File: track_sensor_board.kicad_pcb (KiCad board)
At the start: 2 copper layers, 111.8 x 96.5 mm, 30 parts, among them J1 Barrel_Jack, J10 Screw_Terminal_01x02, J11 Screw_Terminal_01x02, J2 10-18-1032, J3 10-18-1032, J4 10-18-1032, J5 10-18-1032, J6 10-18-1032, J7 10-18-1032, J8 10-18-1032, J9 10-18-1032, SW1 SW_DIP_x04, U1 MCP23017_SP, U2 TSR_1-2450

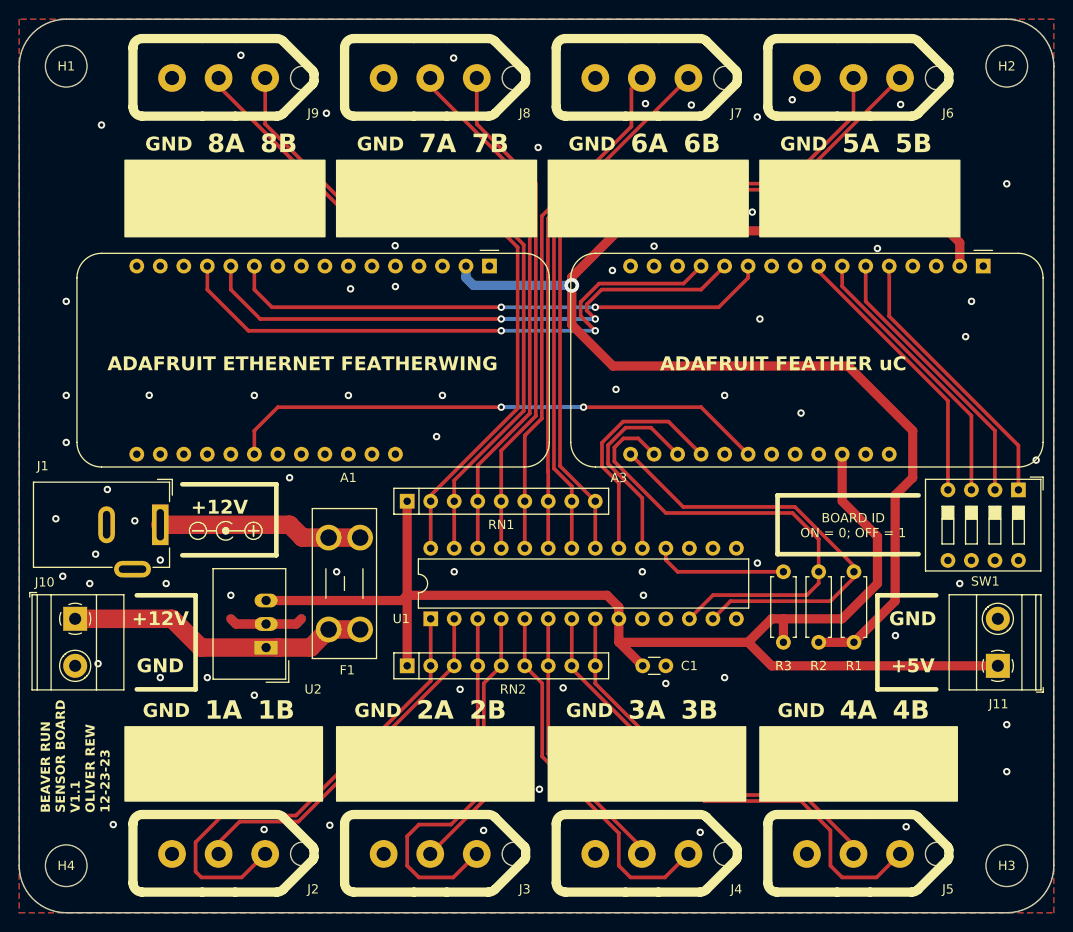
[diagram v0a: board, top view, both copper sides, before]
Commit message: feat: added filter caps
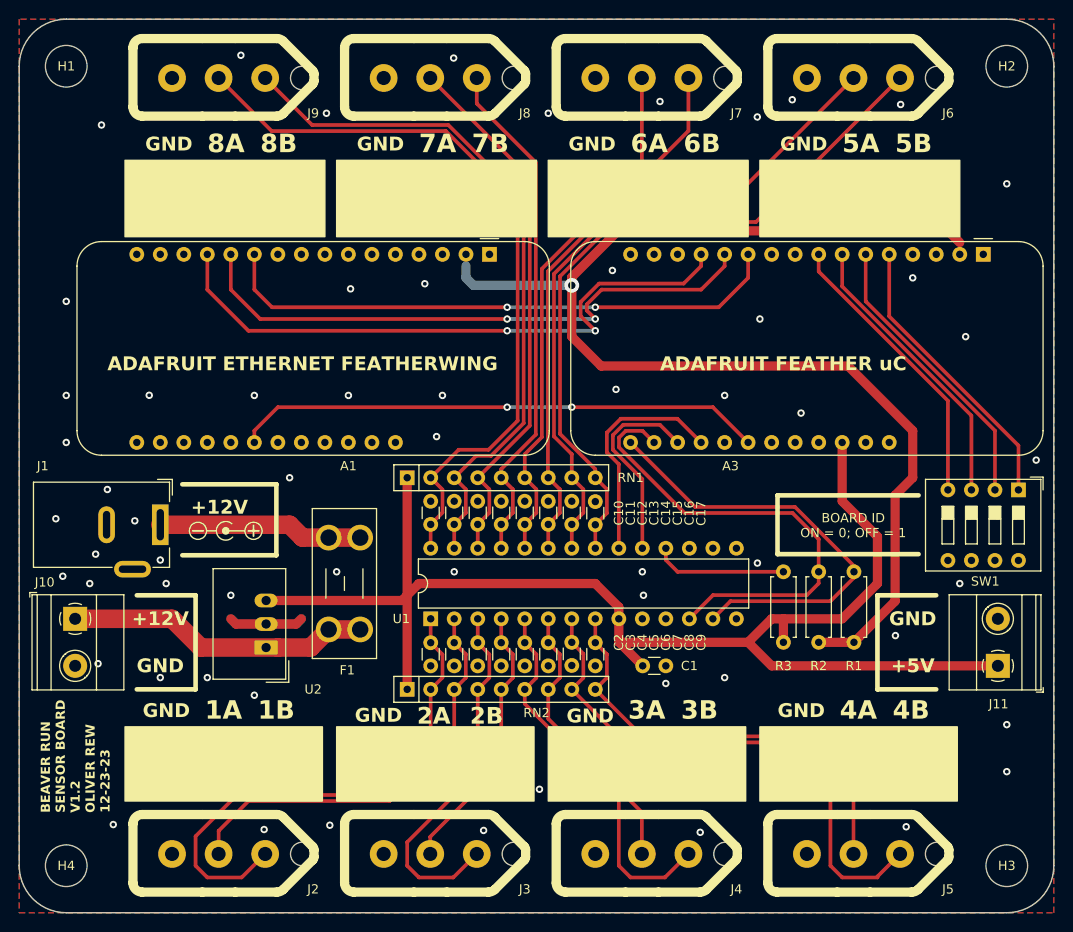
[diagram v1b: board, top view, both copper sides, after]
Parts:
- added C10: 0.1uf, Capacitor_THT:C_Disc_D3.0mm_W1.6mm_P2.50mm, F.Cu at (135.9, 102.8)
- added C11: 0.1uf, Capacitor_THT:C_Disc_D3.0mm_W1.6mm_P2.50mm, F.Cu at (138.4, 102.8)
- added C12: 0.1uf, Capacitor_THT:C_Disc_D3.0mm_W1.6mm_P2.50mm, F.Cu at (141.0, 102.8)
- added C13: 0.1uf, Capacitor_THT:C_Disc_D3.0mm_W1.6mm_P2.50mm, F.Cu at (143.5, 102.8)
- added C14: 0.1uf, Capacitor_THT:C_Disc_D3.0mm_W1.6mm_P2.50mm, F.Cu at (146.1, 102.8)
- added C15: 0.1uf, Capacitor_THT:C_Disc_D3.0mm_W1.6mm_P2.50mm, F.Cu at (148.6, 102.8)
- added C16: 0.1uf, Capacitor_THT:C_Disc_D3.0mm_W1.6mm_P2.50mm, F.Cu at (151.1, 102.8)
- added C17: 0.1uf, Capacitor_THT:C_Disc_D3.0mm_W1.6mm_P2.50mm, F.Cu at (153.7, 102.9)
- added C2: 0.1uf, Capacitor_THT:C_Disc_D3.0mm_W1.6mm_P2.50mm, F.Cu at (135.9, 115.6)
- added C3: 0.1uf, Capacitor_THT:C_Disc_D3.0mm_W1.6mm_P2.50mm, F.Cu at (138.4, 115.6)
- added C4: 0.1uf, Capacitor_THT:C_Disc_D3.0mm_W1.6mm_P2.50mm, F.Cu at (141.0, 115.6)
- added C5: 0.1uf, Capacitor_THT:C_Disc_D3.0mm_W1.6mm_P2.50mm, F.Cu at (143.5, 115.6)
- added C6: 0.1uf, Capacitor_THT:C_Disc_D3.0mm_W1.6mm_P2.50mm, F.Cu at (146.1, 115.6)
- added C7: 0.1uf, Capacitor_THT:C_Disc_D3.0mm_W1.6mm_P2.50mm, F.Cu at (148.6, 115.6)
- added C8: 0.1uf, Capacitor_THT:C_Disc_D3.0mm_W1.6mm_P2.50mm, F.Cu at (151.1, 115.6)
- added C9: 0.1uf, Capacitor_THT:C_Disc_D3.0mm_W1.6mm_P2.50mm, F.Cu at (153.7, 115.6)
- moved RN2 2.54 mm to (133.3, 120.7)
- moved RN1 2.54 mm to (133.3, 97.8)
- moved A1 1.27 mm to (142.2, 73.7)
- moved A3 1.27 mm to (195.6, 73.7)
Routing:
- net +5V: track 140.8 -> 148.2 mm
- net Net-(RN2-R2): track 39.7 -> 45.9 mm
- net Net-(RN2-R7): track 53.5 -> 59.1 mm
- net Net-(RN2-R1): track 51.3 -> 56.8 mm
- net Net-(RN1-R1): track 76.8 -> 82.0 mm
- net Net-(RN1-R7): track 77.3 -> 72.6 mm
- net Net-(RN2-R8): track 43.1 -> 47.7 mm
- net Net-(A1-SCK): track 59.3 -> 61.8 mm
- net Net-(A1-MOSI): track 61.8 -> 64.3 mm
- net Net-(A1-MISO): track 64.7 -> 67.2 mm
- net Net-(RN1-R8): track 79.9 -> 77.6 mm
- net Net-(RN1-R2): track 74.2 -> 76.1 mm
- net +3.3V: track 136.1 -> 134.3 mm
- net Net-(A1-CS): track 59.0 -> 57.2 mm
- net Net-(A3-DAC0/A0): track 30.0 -> 31.2 mm
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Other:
- board text added: "BEAVER RUN SENSOR BOARD V1.2 OLIVER REW 12-23-23"
- board text removed: "BEAVER RUN SENSOR BOARD V1.1 OLIVER REW 12-23-23"

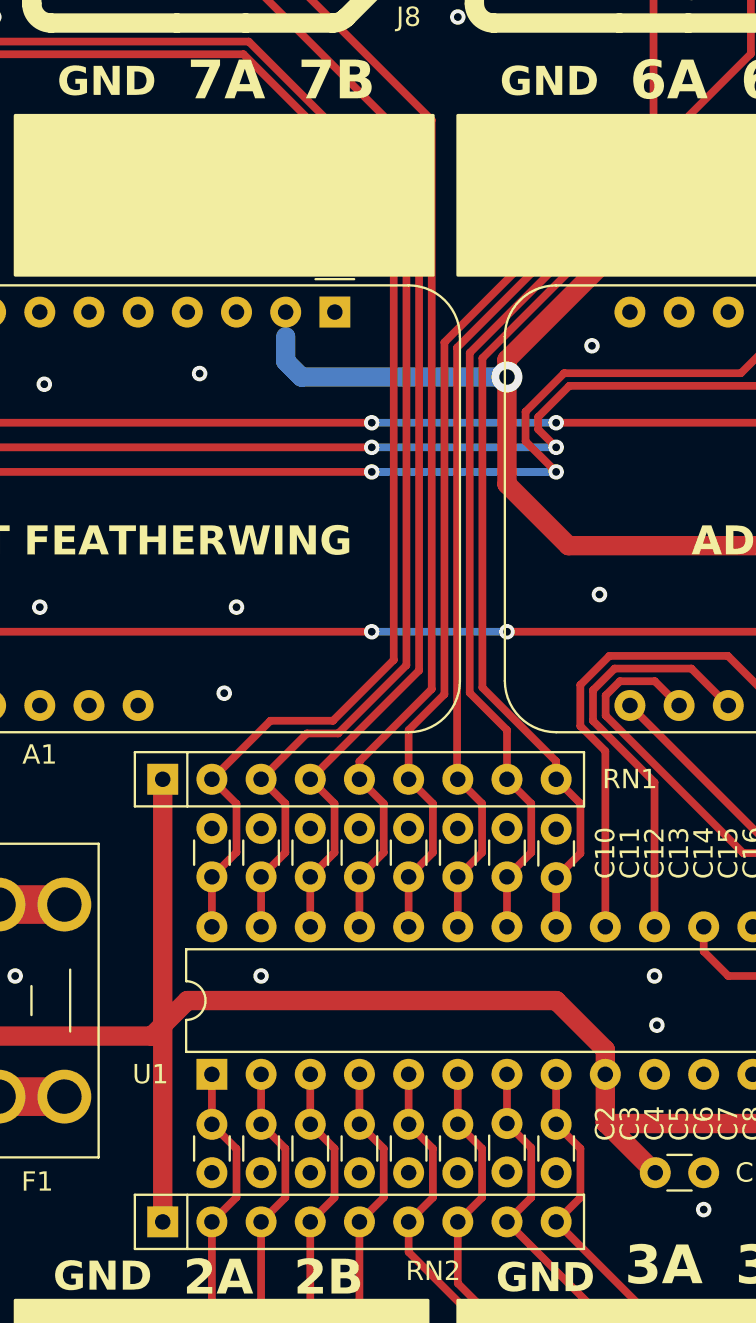
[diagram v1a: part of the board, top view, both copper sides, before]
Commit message: fix: fix grounds on caps
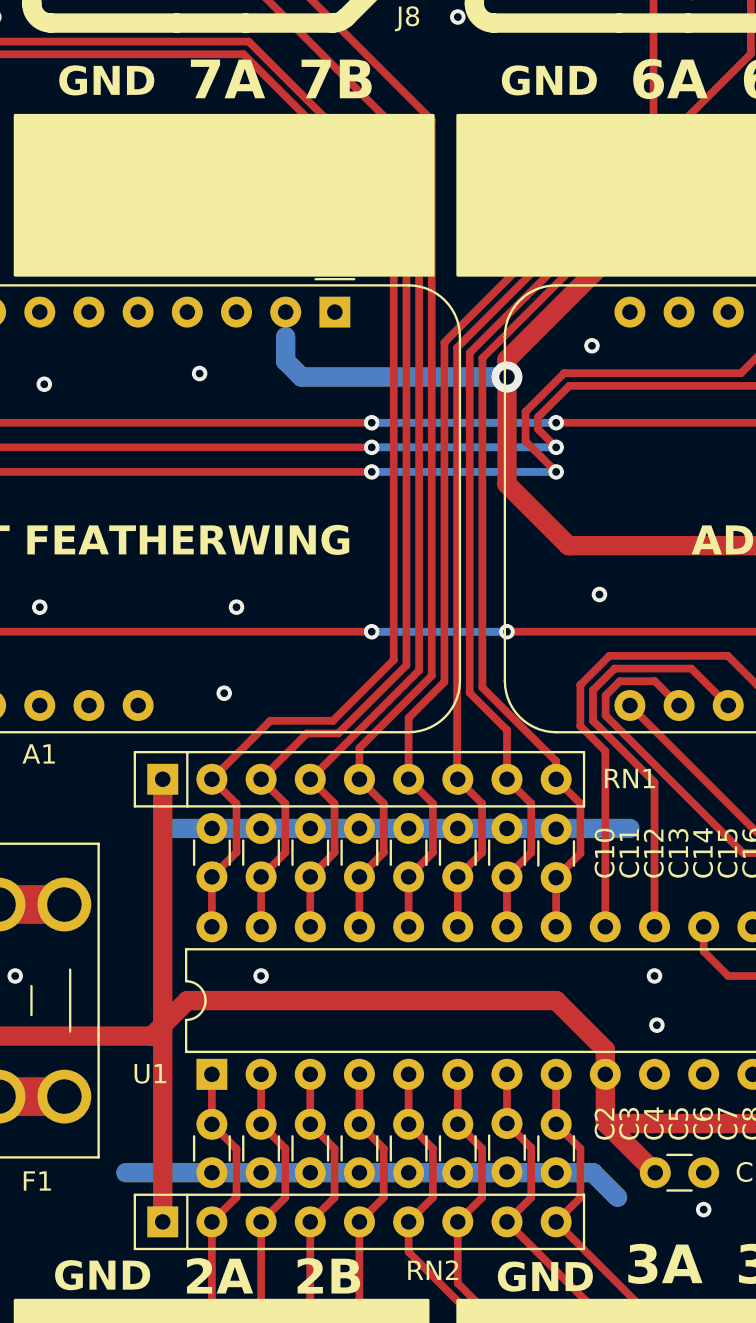
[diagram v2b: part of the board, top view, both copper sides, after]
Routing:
- net GND: track 16.2 -> 66.2 mm
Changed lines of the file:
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@@
   (via (at 96.52 93.98) (size 0.8) (drill 0.4) (layers "F.Cu" "B.Cu") (free) (net 2))
   (via (at 198.12 124.46) (size 0.8) (drill 0.4) (layers "F.Cu" "B.Cu") (free) (net 2))
+  (segment (start 155.575 118.11) (end 156.845 119.38) (width 1) (layer "B.Cu") (net 2))
   (segment (start 114.863728 113.593728) (end 118.11 113.593728) (width 1) (layer "B.Cu") (net 2))
+  (segment (start 135.89 100.33) (end 157.48 100.33) (width 1) (layer "B.Cu") (net 2))
+  (segment (start 135.89 118.11) (end 155.575 118.11) (width 1) (layer "B.Cu") (net 2))
+  (segment (start 135.89 118.11) (end 131.445 118.11) (width 1) (layer "B.Cu") (net 2))
   (segment (start 114.863728 113.593728) (end 114.3 113.03) (width 1) (layer "B.Cu") (net 2))
   (segment (start 121.356272 113.593728) (end 121.92 113.03) (width 1) (layer "B.Cu") (net 2))
+  (segment (start 135.89 100.33) (end 133.35 100.33) (width 1) (layer "B.Cu") (net 2))
   (segment (start 121.356272 113.593728) (end 118.11 113.593728) (width 1) (layer "B.Cu") (net 2))
   (segment (start 144.145 79.375) (end 118.745 79.375) (width 0.4) (layer "F.Cu") (net 3))
@@
   (segment (start 148.59 102.83) (end 148.59 105.41) (width 0.4) (layer "F.Cu") (net 35))
   (segment (start 148.552 97.752) (end 148.552 75.498028) (width 0.4) (layer "F.Cu") (net 35))
+  (segment (start 146.05 94.615) (end 147.898 92.767) (width 0.4) (layer "F.Cu") (net 36))
   (segment (start 147.304 99.044) (end 147.304 101.576) (width 0.4) (layer "F.Cu") (net 36))
+  (segment (start 146.05 102.83) (end 146.05 105.41) (width 0.4) (layer "F.Cu") (net 36))
+  (segment (start 147.898 92.767) (end 147.898 75.227132) (width 0.4) (layer "F.Cu") (net 36))
+  (segment (start 146.05 97.79) (end 146.05 94.615) (width 0.4) (layer "F.Cu") (net 36))
+  (segment (start 147.304 101.576) (end 146.05 102.83) (width 0.4) (layer "F.Cu") (net 36))
+  (segment (start 158.6992 64.425932) (end 158.6992 54.61) (width 0.4) (layer "F.Cu") (net 36))
   (segment (start 147.898 75.227132) (end 158.6992 64.425932) (width 0.4) (layer "F.Cu") (net 36))
-  (segment (start 146.05 102.83) (end 146.05 105.41) (width 0.4) (layer "F.Cu") (net 36))
-  (segment (start 158.6992 64.425932) (end 158.6992 54.61) (width 0.4) (layer "F.Cu") (net 36))
-  (segment (start 146.05 95.25) (end 147.898 93.402) (width 0.4) (layer "F.Cu") (net 36))
-  (segment (start 147.304 101.576) (end 146.05 102.83) (width 0.4) (layer "F.Cu") (net 36))
-  (segment (start 147.898 93.402) (end 147.898 75.227132) (width 0.4) (layer "F.Cu") (net 36))
-  (segment (start 146.05 97.79) (end 146.05 95.25) (width 0.4) (layer "F.Cu") (net 36))
   (segment (start 146.05 97.79) (end 147.304 99.044) (width 0.4) (layer "F.Cu") (net 36))
   (segment (start 140.8684 57.3659) (end 140.8684 54.61) (width 0.4) (layer "F.Cu") (net 37))
+  (segment (start 143.51 96.174896) (end 147.244 92.440896) (width 0.4) (layer "F.Cu") (net 37))
   (segment (start 147.244 63.7415) (end 140.8684 57.3659) (width 0.4) (layer "F.Cu") (net 37))
   (segment (start 144.764 101.576) (end 143.51 102.83) (width 0.4) (layer "F.Cu") (net 37))
   (segment (start 143.51 97.79) (end 144.764 99.044) (width 0.4) (layer "F.Cu") (net 37))
+  (segment (start 147.244 92.440896) (end 147.244 63.7415) (width 0.4) (layer "F.Cu") (net 37))
+  (segment (start 143.51 97.79) (end 143.51 96.174896) (width 0.4) (layer "F.Cu") (net 37))
   (segment (start 143.51 102.83) (end 143.51 105.41) (width 0.4) (layer "F.Cu") (net 37))
   (segment (start 144.764 99.044) (end 144.764 101.576) (width 0.4) (layer "F.Cu") (net 37))
-  (segment (start 143.51 97.79) (end 143.51 96.865104) (width 0.4) (layer "F.Cu") (net 37))
-  (segment (start 147.244 93.131104) (end 147.244 63.7415) (width 0.4) (layer "F.Cu") (net 37))
-  (segment (start 143.51 96.865104) (end 147.244 93.131104) (width 0.4) (layer "F.Cu") (net 37))
   (segment (start 146.59 92.17) (end 146.59 65.3608) (width 0.4) (layer "F.Cu") (net 38))
   (segment (start 140.97 97.79) (end 146.59 92.17) (width 0.4) (layer "F.Cu") (net 38))

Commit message: feat: one last fix before gerbers
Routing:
- net GND: vias 60 -> 61
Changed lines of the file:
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@@
   (via (at 116.84 88.9) (size 0.8) (drill 0.4) (layers "F.Cu" "B.Cu") (free) (net 2))
   (via (at 111.76 119.38) (size 0.8) (drill 0.4) (layers "F.Cu" "B.Cu") (free) (net 2))
+  (via (at 172.085 97.79) (size 0.8) (drill 0.4) (layers "F.Cu" "B.Cu") (free) (net 2))
   (via (at 101.6 135.255) (size 0.8) (drill 0.4) (layers "F.Cu" "B.Cu") (free) (net 2))
   (via (at 116.84 121.285) (size 0.8) (drill 0.4) (layers "F.Cu" "B.Cu") (free) (net 2))
